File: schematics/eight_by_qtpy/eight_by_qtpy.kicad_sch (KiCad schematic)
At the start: 44 parts, among them J1 Conn_01x08, SW1 SW_Push_45deg, SW2 SW_Push_45deg, SW3 SW_Push_45deg, SW4 SW_Push_45deg, SW5 SW_Push_45deg, SW6 SW_Push_45deg, SW7 SW_Push_45deg, SW8 SW_Push_45deg, U1 74HC4051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

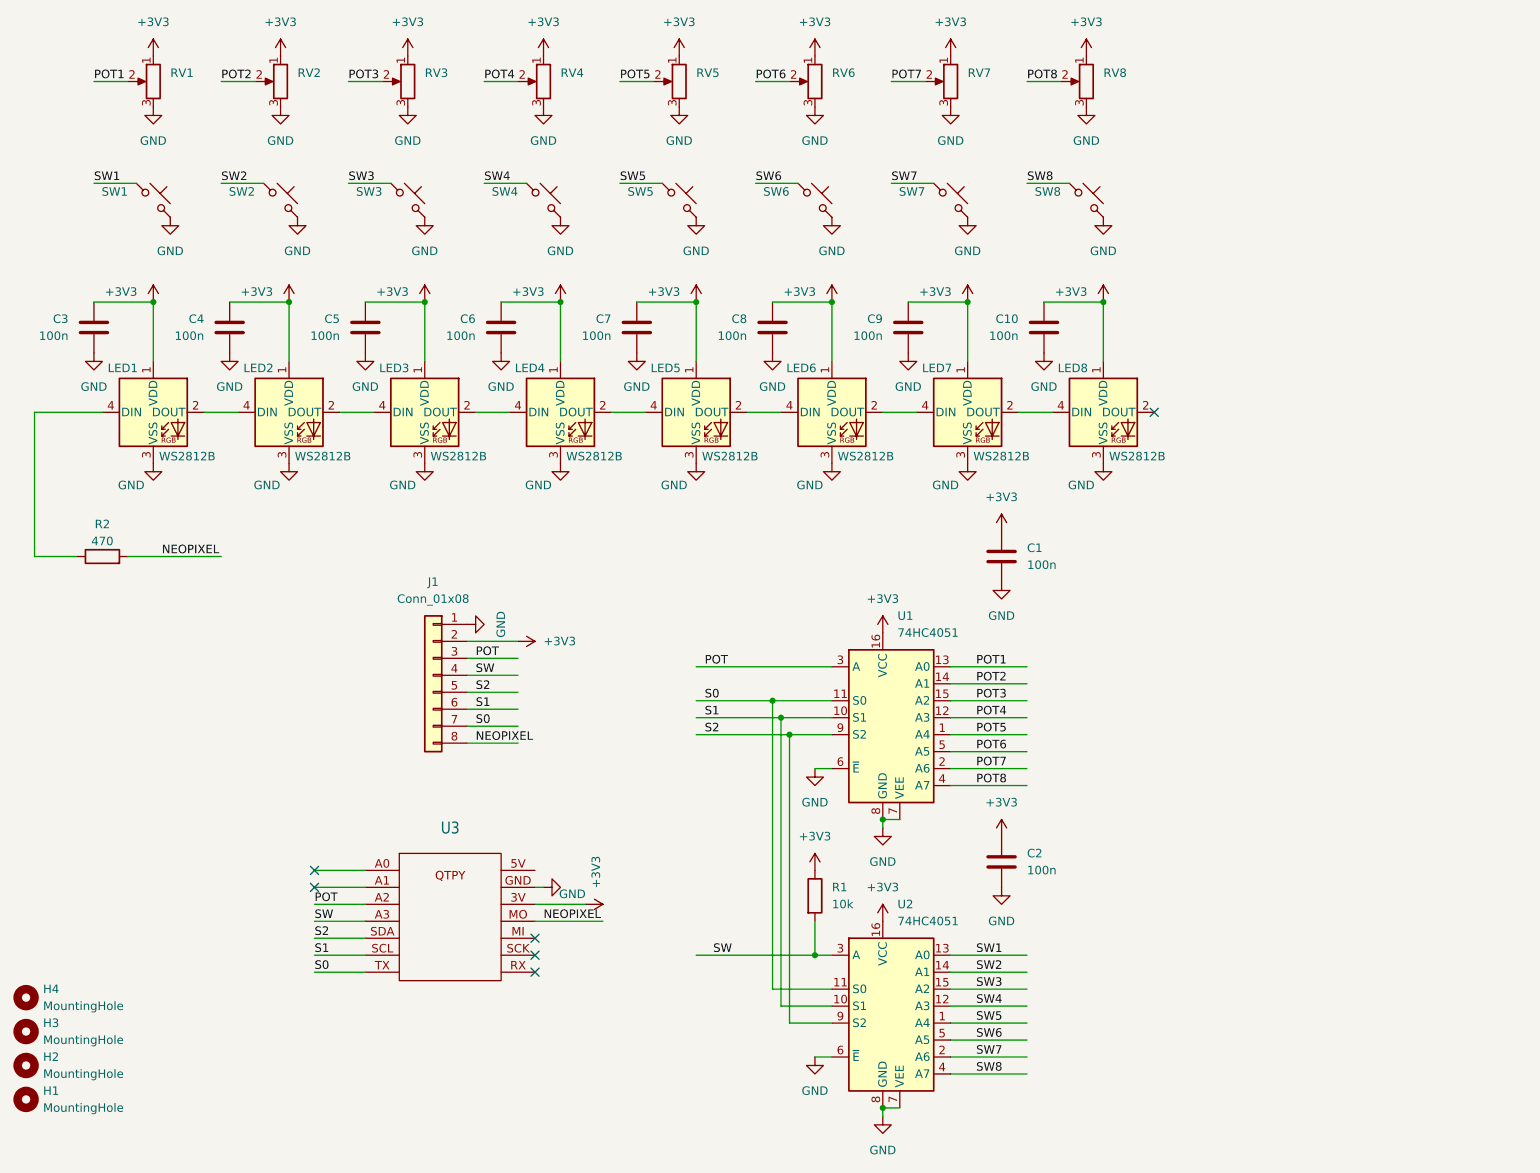
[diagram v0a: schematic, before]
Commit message: add two extra buttons & LEDs if using a QTpy
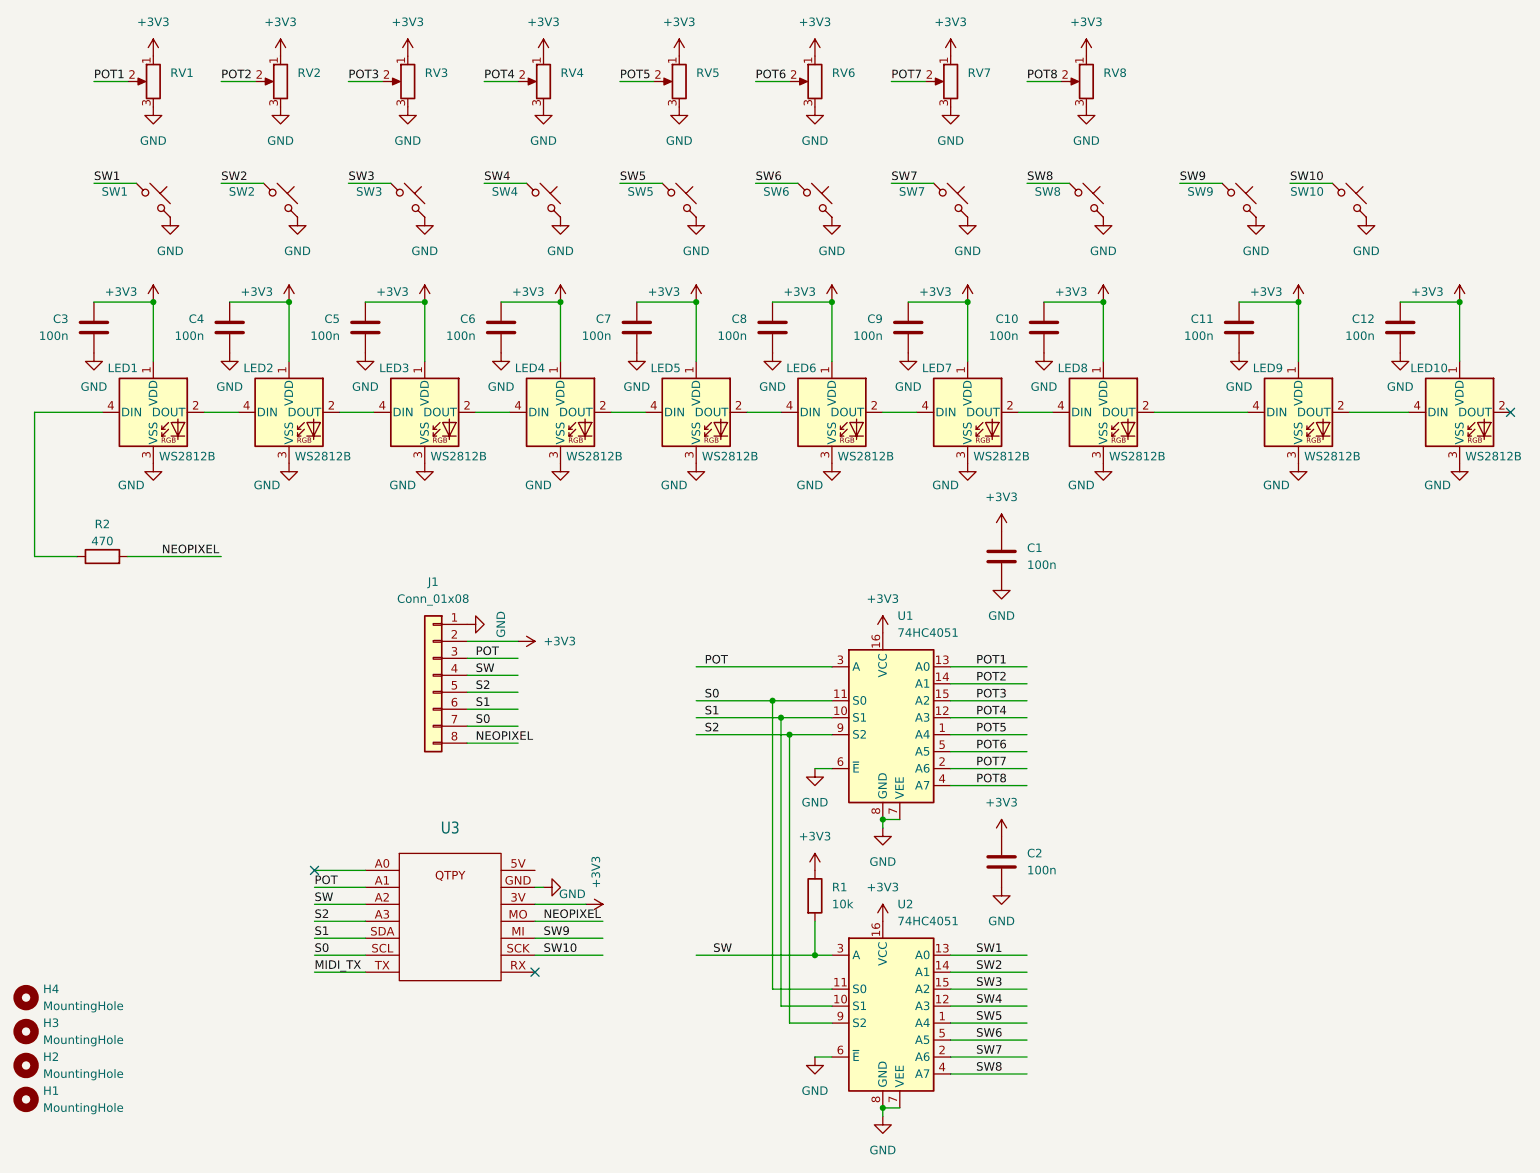
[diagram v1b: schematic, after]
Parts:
- added C11, C12: 100n, Capacitor_SMD:C_0603_1608Metric, symbol Device:C
- added LED10, LED9: WS2812B, LED_SMD:LED_WS2812B-Mini_PLCC4_3.5x3.5mm, symbol LED:WS2812B
- added SW10, SW9: SW_Push_45deg, Button_Switch_THT:SW_PUSH_6mm_H7.3mm, symbol Switch:SW_Push_45deg
- U3: footprint todbot_eagle2023:QTPY_TH -> todbot_eagle2023:QTPY_TH_HEADERSOCKET
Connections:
- net +3V3: now also C11.1, C12.1, LED10.1 (VDD), LED9.1 (VDD)
- net GND: now also C11.2, C12.2, LED10.3 (VSS), LED9.3 (VSS), SW10.1, SW9.1
- net POT: now also U3.A1 (9); no longer U3.A2
- net S0: now also U3.SCL; no longer U3.TX
- net S1: now also U3.SDA; no longer U3.SCL
- net S2: now also U3.A3; no longer U3.SDA
- net SW: now also U3.A2; no longer U3.A3
- net SW9: now reaches U3.MI
- net SW9: now also SW9.2
- net SW10: now reaches U3.SCK
- net SW10: now also SW10.2
- net at LED8.2 (DOUT): now also LED9.4 (DIN)
- new net: LED10.4 (DIN), LED9.2 (DOUT)
- new net MIDI_TX: U3.TX
- no-connect marks 6 -> 3

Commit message: clean up
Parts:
- added J2: AudioJack4, todbot_stuff:Jack_3.5mm_PJ320D_Horizontal, symbol Connector_Audio:AudioJack4
- added R3: 10, Resistor_SMD:R_0603_1608Metric, symbol Device:R
- added R4: 33, Resistor_SMD:R_0603_1608Metric, symbol Device:R
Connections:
- net +3V3: now also R4.2
- net GND: now also J2.S
- net MIDI_TX renamed MIDI_OUT
- net MIDI_OUT: now also R3.2
- new net: J2.R1, R4.1
- new net: J2.T, R3.1
- no-connect marks 3 -> 4

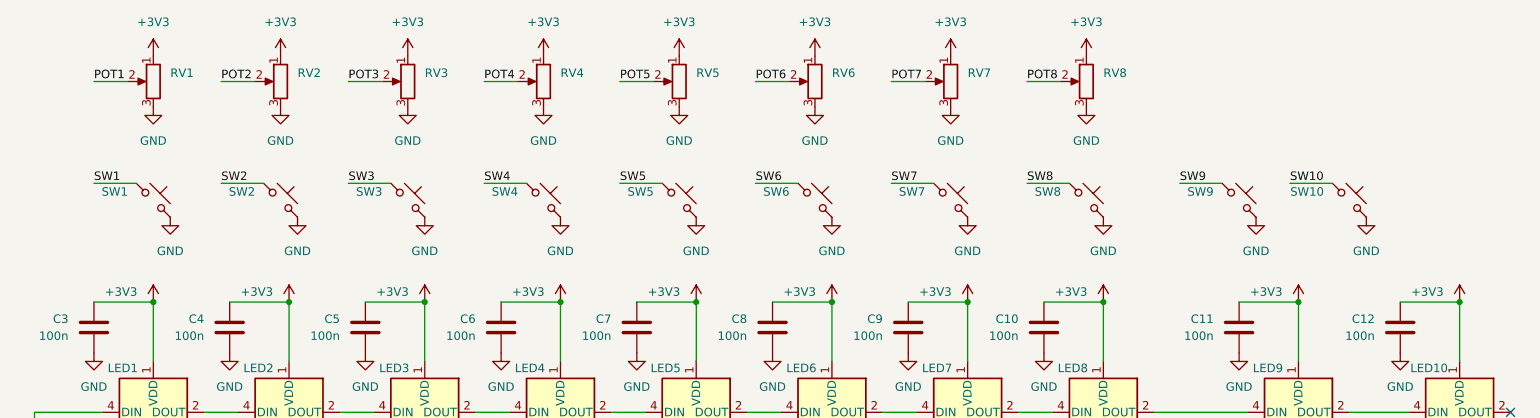
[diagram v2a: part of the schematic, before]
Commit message: refactor eight_by_qtpy to use 12mm switches instead of std 6mm tact
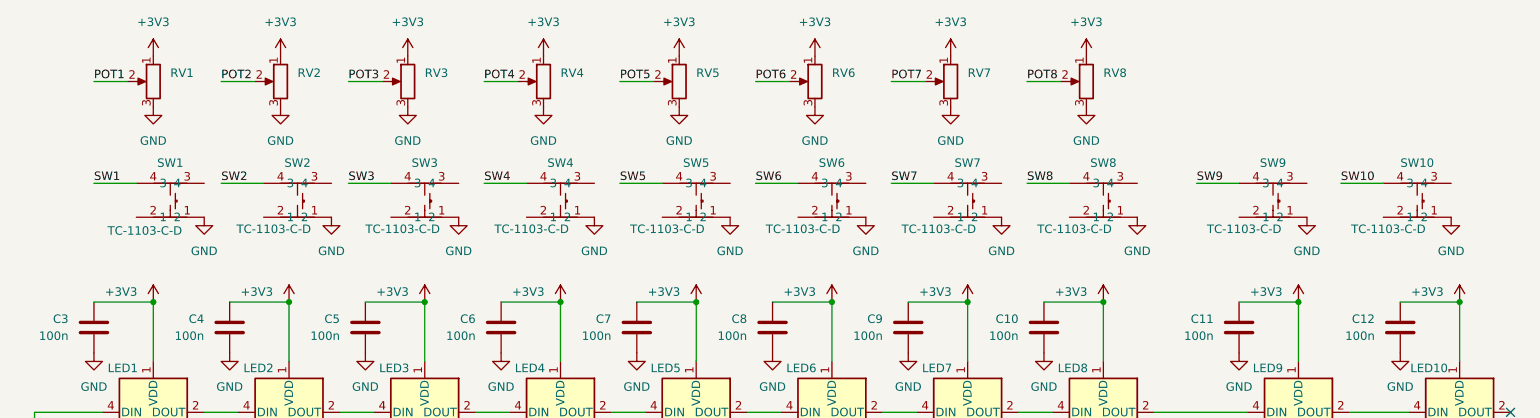
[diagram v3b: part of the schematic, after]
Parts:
- removed SW1, SW10, SW2, SW3, SW4, SW5, SW6, SW7, SW8, SW9: SW_Push_45deg, Button_Switch_THT:SW_PUSH_6mm_H7.3mm, symbol Switch:SW_Push_45deg
- added SW1, SW10, SW2, SW3, SW4, SW5, SW6, SW7, SW8, SW9: TC-1103-C-D, easyeda2kicad:SW-TH_4P-L12.0-W12.0-P5.00-LS12.5, symbol easyeda2kicad:TC-1103-C-D
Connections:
- net GND: now also SW1.1, SW10.1, SW2.1, SW3.1, SW4.1, SW5.1, SW6.1, SW7.1, SW8.1, SW9.1
- net SW1: now also SW1.4
- net SW10: now also SW10.4
- net SW2: now also SW2.4
- net SW3: now also SW3.4
- net SW4: now also SW4.4
- net SW5: now also SW5.4
- net SW6: now also SW6.4
- net SW7: now also SW7.4
- net SW8: now also SW8.4
- net SW9: now also SW9.4
